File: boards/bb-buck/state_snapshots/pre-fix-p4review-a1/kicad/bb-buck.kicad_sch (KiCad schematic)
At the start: 22 parts, among them J1 KF128-5.08-2P, J2 KF128-5.08-2P, U1 LMR33630ADDAR

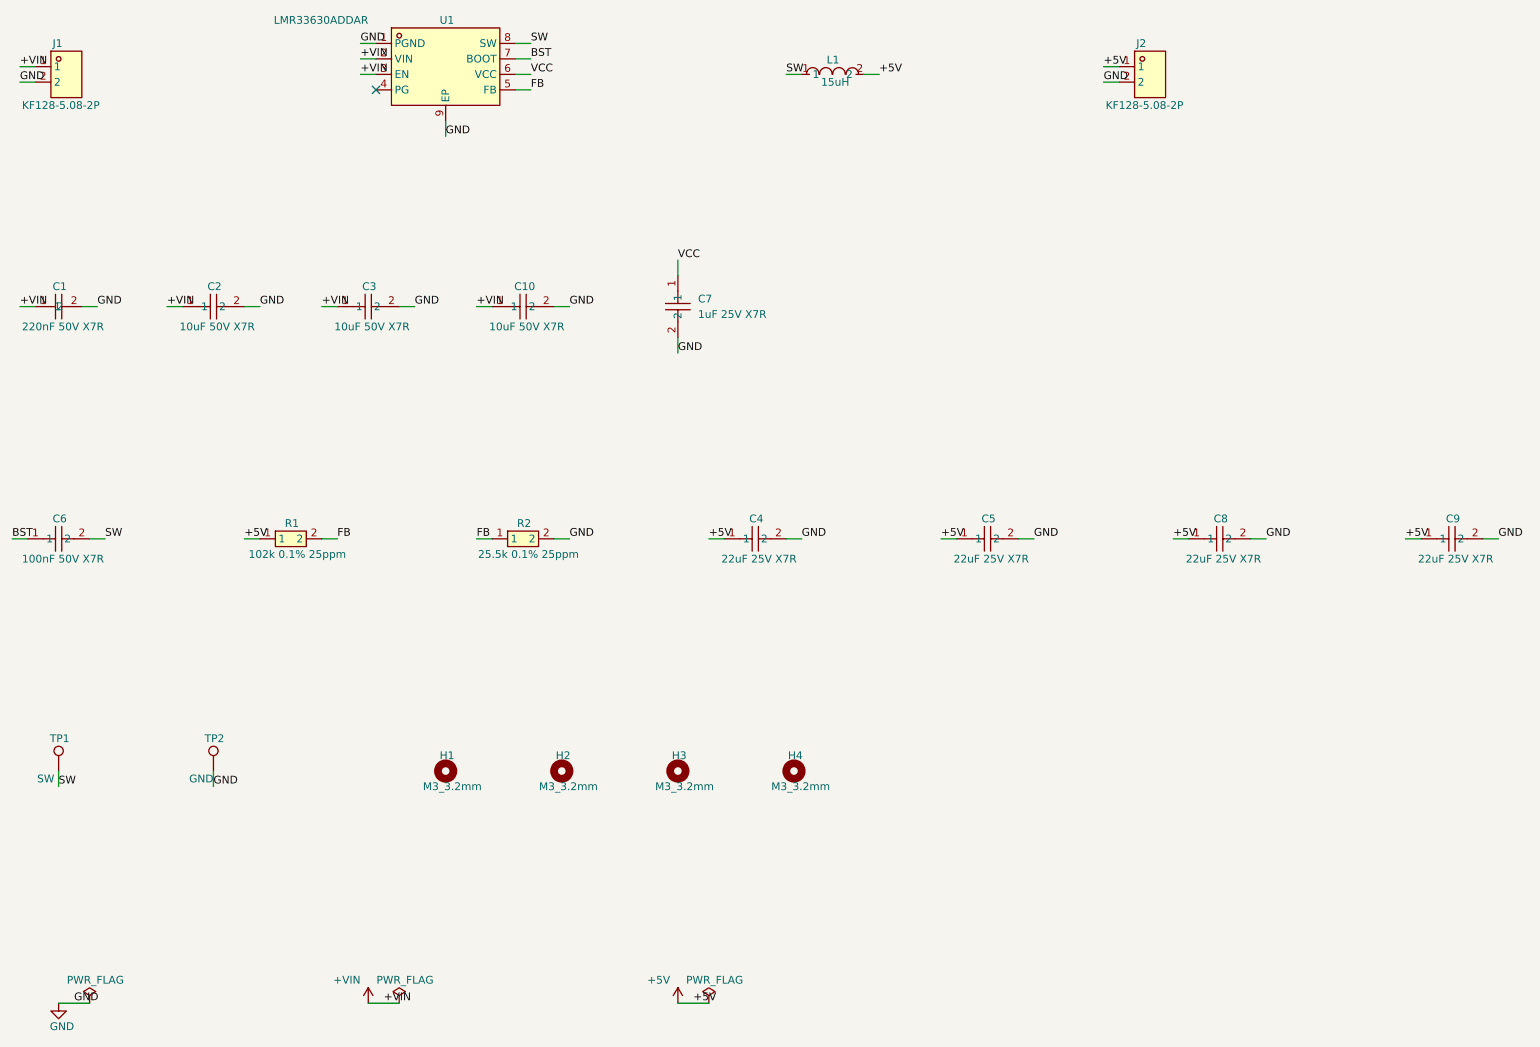
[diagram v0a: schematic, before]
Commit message: ai-ee bb-buck: erc pass (post-review fix: 4x22uF Cout, 3x10uF Cin, divider recentred)
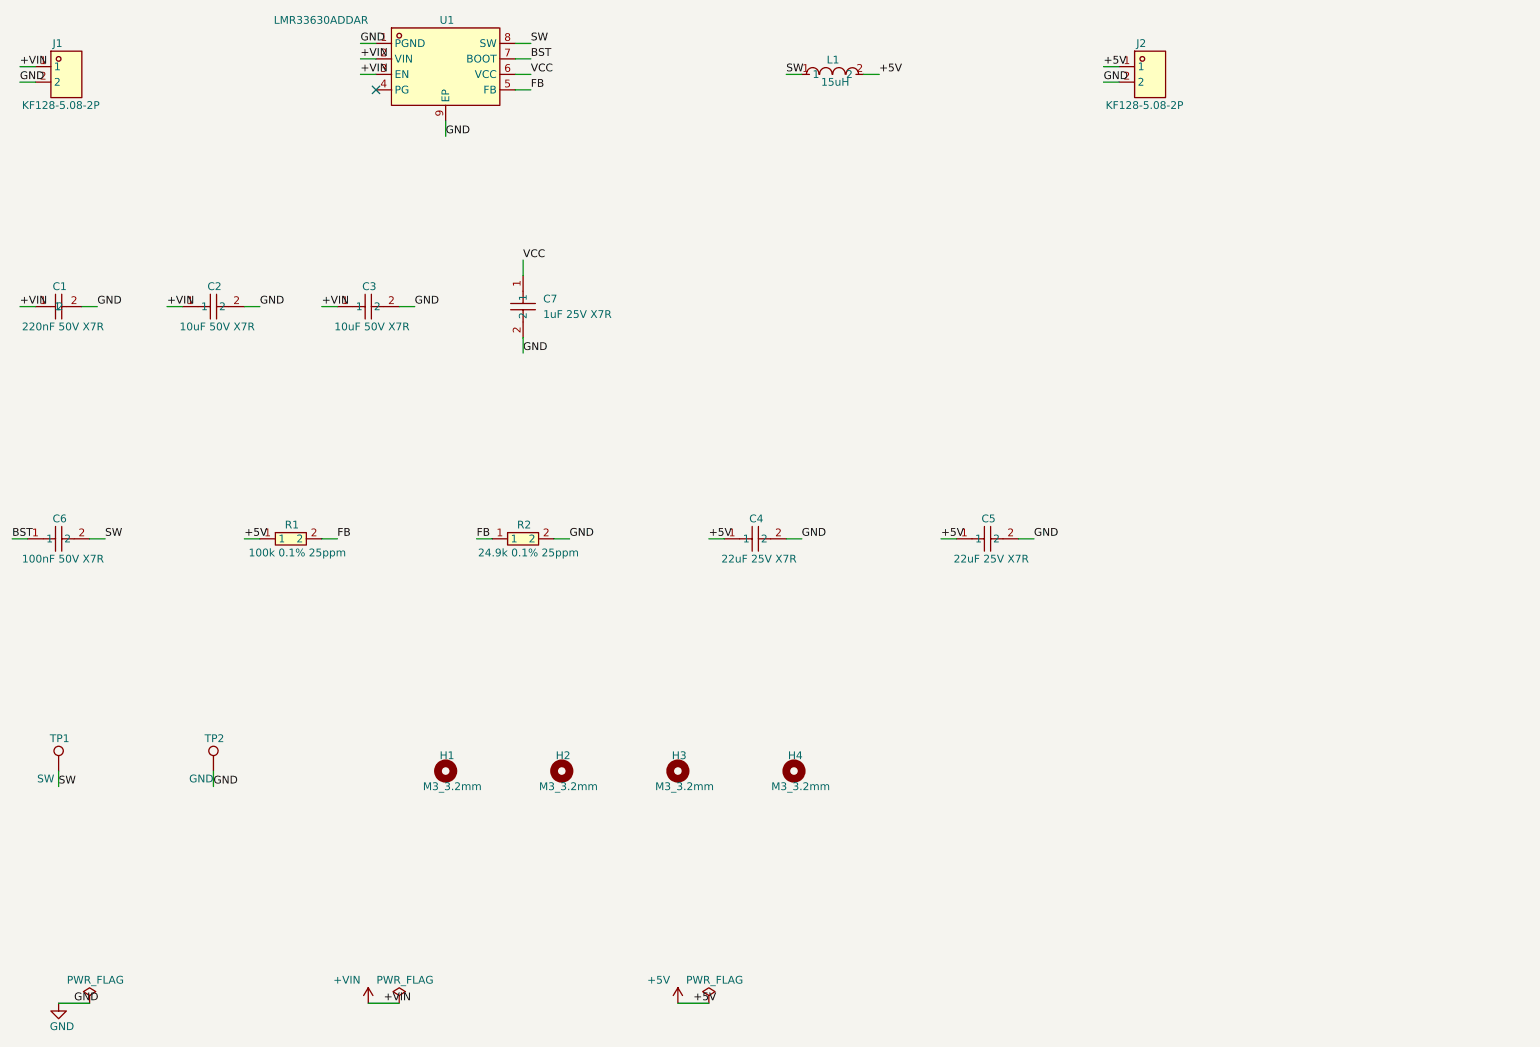
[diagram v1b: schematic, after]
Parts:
- removed C10: 10uF 50V X7R, aiee:C1210, symbol aiee:CS3225X7R106K500NRL
- removed C8, C9: 22uF 25V X7R, aiee:C1210, symbol aiee:CS3225X7R226K250NRL
- removed R1: 102k 0.1% 25ppm, aiee:R0603, symbol aiee:RT0603BRD07102KL
- removed R2: 25.5k 0.1% 25ppm, aiee:R0603, symbol aiee:RT0603BRD0725K5L
- added R1: 100k 0.1% 25ppm, aiee:R0603, symbol aiee:RT0603BRD07100KL
- added R2: 24.9k 0.1% 25ppm, aiee:R0603, symbol aiee:RT0603BRD0724K9L
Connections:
- net +5V: now also R1.1
- net FB: now also R1.2, R2.1
- net GND: now also R2.2
